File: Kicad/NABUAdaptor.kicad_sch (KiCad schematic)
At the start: 102 parts, among them J1 Conn_01x04, J2 DIN-5_180degree, J3 Conn_01x09, J4 Conn_01x05, U1 74LS164, U10 UA9638CD, U11 UA9637, U12 74LS164, U13 74LS164, U14 74LS04, U15 74LS74, U16 N8X60, U17 2114, U18 2114, U19 LM339, U2 74LS30, U20 74LS164, U21 74LS86, U22 74LS74, U23 74LS00, U24 74LS04, U25 74LS00, U26 74LS74, U27 74LS00, U28 74LS74, U29 74LS74, U3 74LS27, U30 74LS02, U31 MC6805P2, U32 74LS74, U33 74HCU04, U4 74LS164, U5 PAL16R6 (ID PAL), U6 74LS374, U7 74LS373, U8 ?VALUE?, U9 TR1865PL, Y1 3.579545MHz

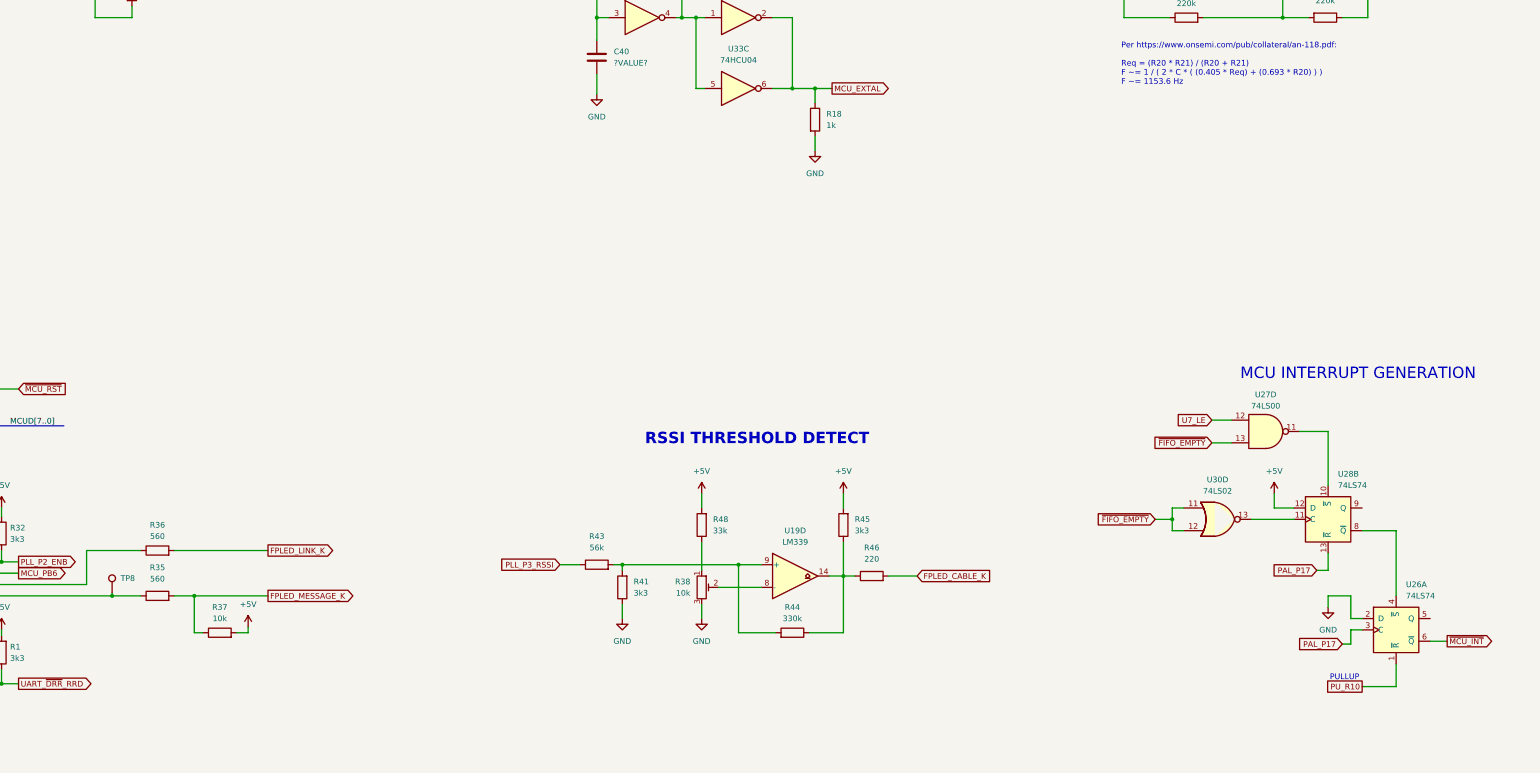
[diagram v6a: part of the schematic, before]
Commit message: sch: move interrupt logic closer to MCU
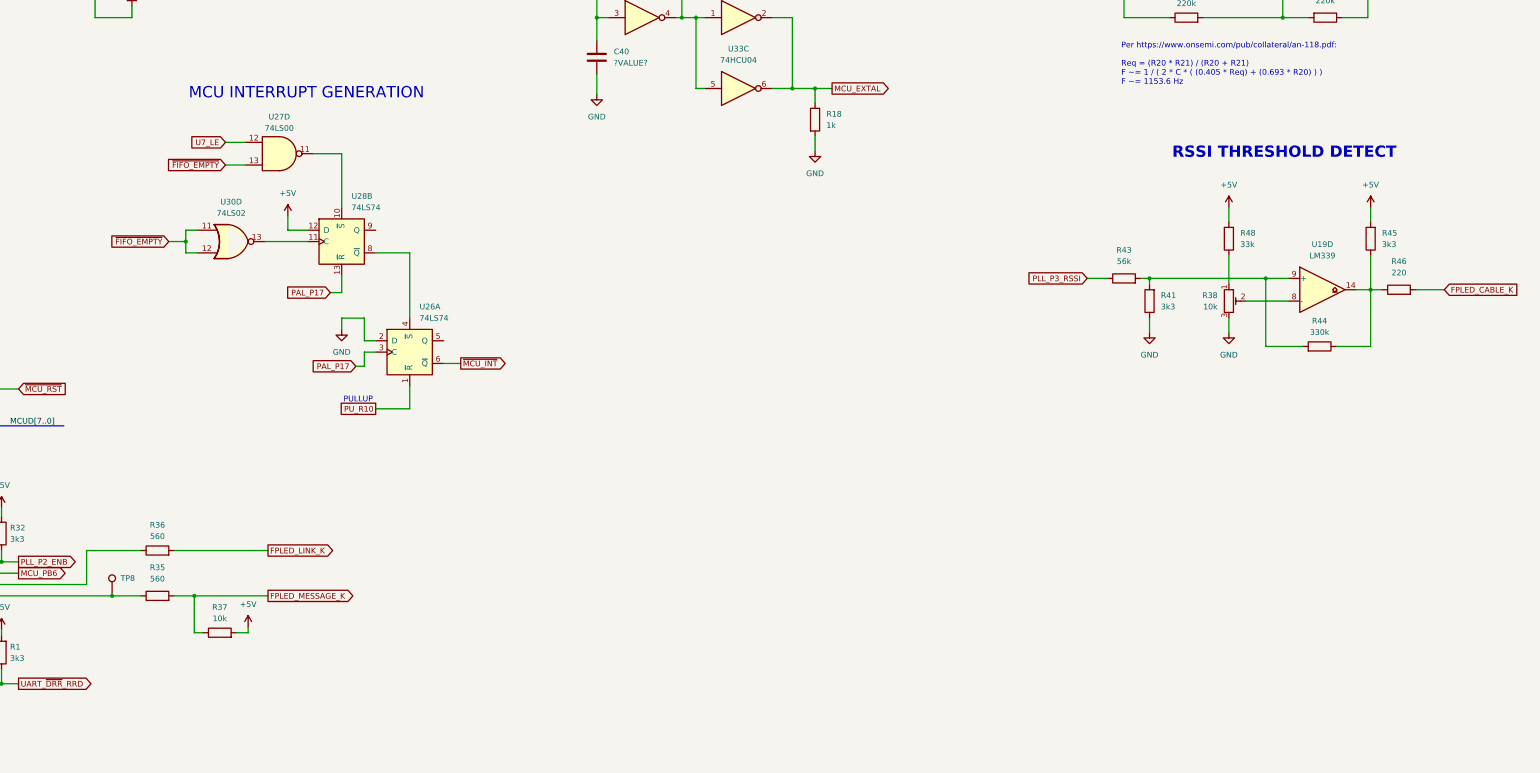
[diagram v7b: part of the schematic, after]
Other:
- moved on the sheet: R38, R41, R43, R44, R45, R46, R48, U19D, U26A, U27D, U28B, U30D

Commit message: add more comp values, C40, and PAL pin names
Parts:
- added C39: 22p, symbol Device:C
- C38: value ?VALUE? -> 100n
- C40: value ?VALUE? -> 22p
- C8: value ?VALUE? -> 10uF 35V
- U8: value ?VALUE? -> 3k3
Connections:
- net GND: now also C39.2
- net at R34.2, U33.1, U33.4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: now also C39.1
- net PAL_P12 renamed PAL_RXGATE_REQ_Q
- net PAL_P17 renamed PAL_FIFO_SO_SET
- net PAL_P18 renamed ~{PAL_FIFO_SO_CLR}
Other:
- note added: "Per https://www.onsemi.com/pub/collateral/an-118.pdf: Req = (R20 * R21) / (R20 + R21) F ~= 1 / ( 2 * C * ( (0.405 * Req) + (0.693 * R20) ) ) F ~= 1153.6 Hz Measured at 1066 Hz by @sharebrained"
- note removed: "Per https://www.onsemi.com/pub/collateral/an-118.pdf: Req = (R20 * R21) / (R20 + R21) F ~= 1 / ( 2 * C * ( (0.405 * Req) + (0.693 * R20) ) ) F ~= 1153.6 Hz"
- moved on the sheet: C40, R34, U33B, Y1
